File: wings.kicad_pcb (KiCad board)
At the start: 2 copper layers, 147.9 x 119.9 mm, 66 parts

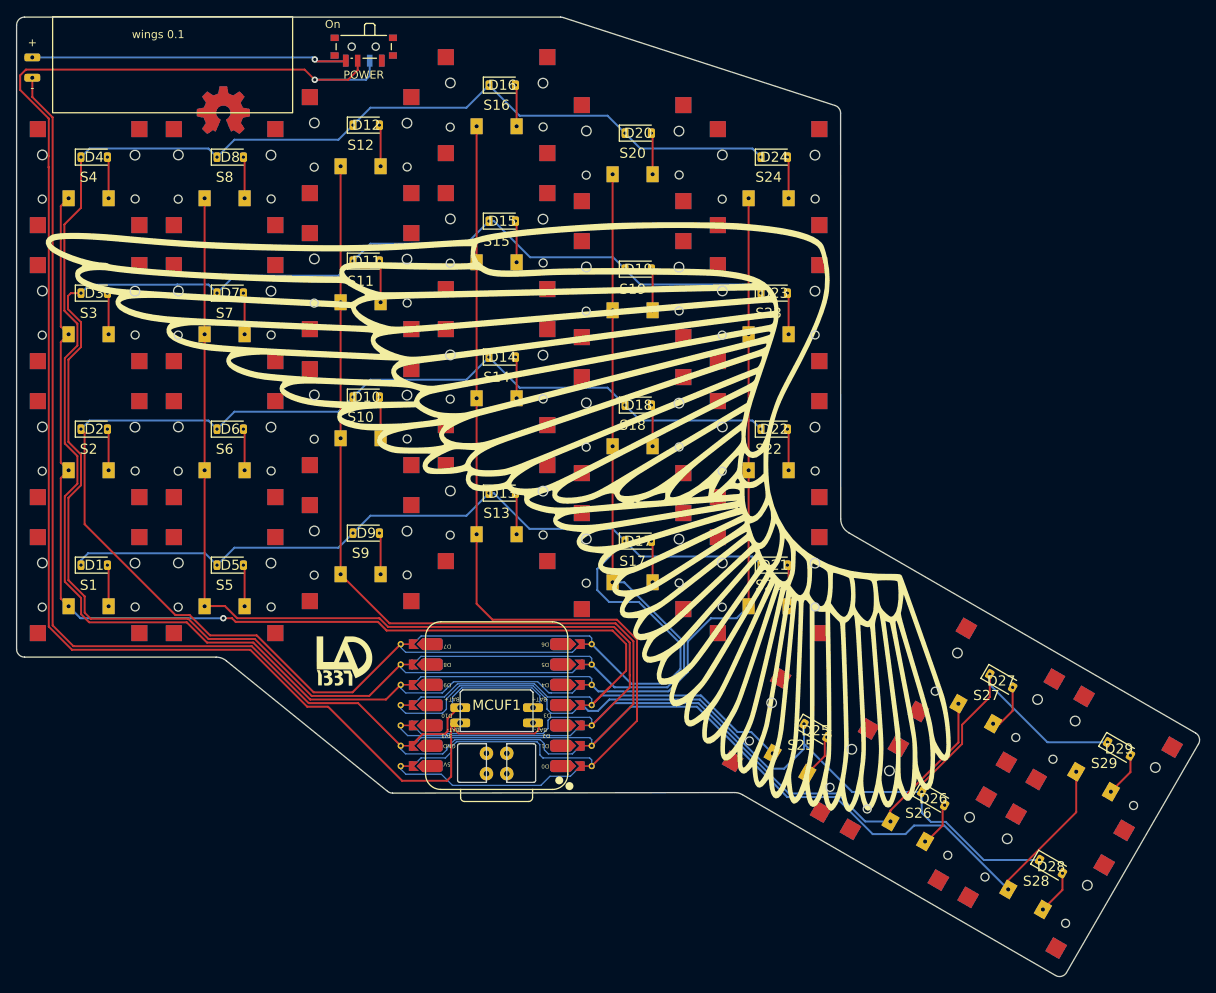
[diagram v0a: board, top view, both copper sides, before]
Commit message: new pcb with fill zone and fixed thumb
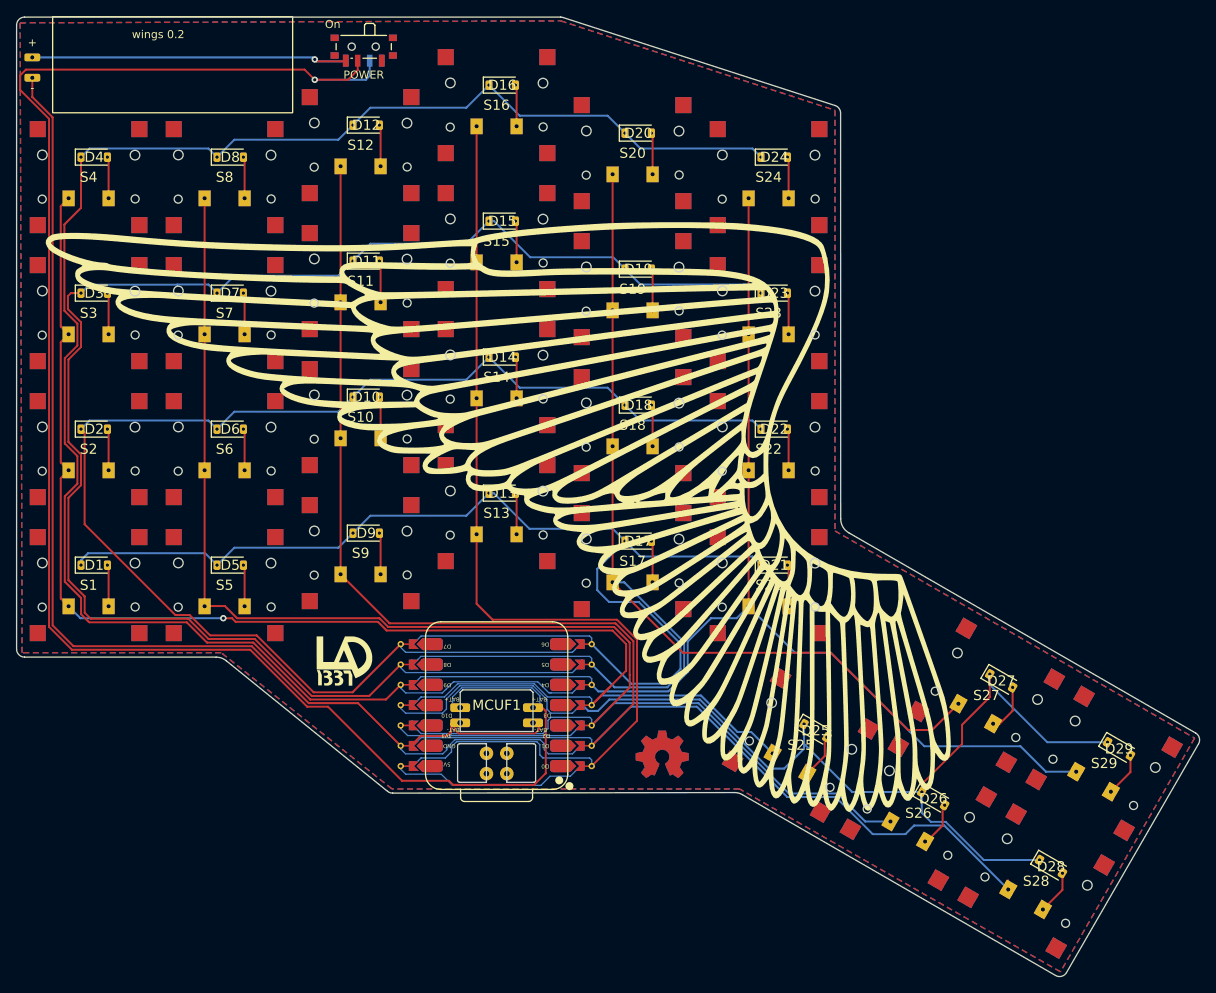
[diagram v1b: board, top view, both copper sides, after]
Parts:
- moved REF** 97.4 mm to (171.7, 121.2) (x2)
- moved G*** 1.27 mm to (130.8, 109.2)
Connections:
- MCUF1 pad 15: GND -> VIN
- MCUF1 pad 16: VIN -> GND
- S27 pad 1: P2 -> P5
- S29 pad 1: P1 -> P4
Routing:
- net P5: track 80.9 -> 133.1 mm
- net P4: track 77.6 -> 127.1 mm
- net P2: track 181.2 -> 163.0 mm
- net P1: track 189.0 -> 171.9 mm
- net VIN: track 190.4 -> 204.7 mm
- net GND: track 128.3 -> 127.3 mm
- added copper zone on B.Cu, net GND
- added copper zone on F.Cu, net GND
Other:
- board text added: "wings 0.2"
- board text removed: "wings 0.1"
